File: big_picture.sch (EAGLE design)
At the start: 66 parts, among them IC1 LM555N

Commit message: updated big picture
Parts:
- removed ADD1, ADD2, BRAKE, HAZ_L, HAZ_R, HEAD, REAR, WIPER: PSMN039-100YS, nxp_60:PSMN039-100YS
- removed ADD1_SWITCH, ADD2_SWITCH, BRAKE_SENSOR, DAY_SWITCH, HAZ_L_SWITCH, HAZ_R_SWITCH, WIPER_SWITCH: (no value), switch:M9040P
- removed ADD2_OUT, ADD2_OUT1, ADD2_OUT2, ADD2_OUT3, ADD2_OUT4, ADD2_OUT5, ADD2_OUT6, ADD2_OUT7, VDD_IN: POWERPOLE_POWER25A, powerpoles:POWERPOLE_POWER25A
- removed C1: 33uF, rcl:C-USC0805
- removed C10, C8, C9: (no value), rcl:C-USC0805
- removed CONTACT: JJM2W-12V, relay:JJM2W-12V
- removed D1: (no value), diode:ZENER-DIODEDO34-7
- removed D2: 1N5817-B, diode:1N5817-B
- removed HORN: TL36WO, switch:TL36WO
- removed IC1: LM555N, linear:LM555N
- removed LED1, LED2, LED3, LED4, LED5, LED6, LED7, LED8: (no value), led:LEDCHIP-LED0805
- removed R1, R11, R2, R20, R21, R3, R4, R5, R6: 10K, rcl:R-US_R0805
- removed R10: 1K, rcl:R-US_R0805
- removed R12, R13, R14, R17, R18, R19, R9: (no value), rcl:R-US_R0805
- removed R15, R16: 220, rcl:R-US_R0805
- removed R7, R8: 0, rcl:R-US_R0805
- removed U$6: HORN, big_picture_parts:HORN
- added DZ1: LZR184, led:LZR184
- added E_STOP1: TL36WO, switch:TL36WO
- added G1: CR1/2, battery:CR1/2
- added K1: RELAY-SPDT-JZC-11F, SparkFun-Electromechanical:RELAY-SPDT-JZC-11F
- added M1: MOTOR10MM, SparkFun-Electromechanical:MOTOR10MM
- added S1: TL37PO, switch:TL37PO
- added SP1: AL30P, buzzer:AL30P
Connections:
- removed net 555_OUT: HAZ_L_SWITCH.P, HAZ_R_SWITCH.P, IC1.Q
- removed net GND: ADD1.S, ADD2.S, BRAKE.S, C1.2, C10.2, C8.2, C9.2, CONTACT2.NO2, D1.A, E_STOP.O, HAZ_L.S, HAZ_R.S, HEAD.S, HORN.O, IC1.GND, R1.2, R2.2, R20.1, R21.1, R3.2, R4.2, R5.2, R6.2, REAR.S, VDD_IN.GND, WIPER.S
- removed net H1: BRAKE_SENSOR.O, R17.1
- removed net H2: HAZ_R_SWITCH.O, R16.1
- removed net H3: HAZ_L_SWITCH.O, R15.1
- removed net H4: R14.1, WIPER_SWITCH.O
- removed net H5: ADD1_SWITCH.O, R13.1
- removed net H6: ADD2_SWITCH.O, R12.1
- removed net H7: DAY_SWITCH.O, R18.1, R19.1
- removed net N$10: LED7.C, R21.2
- removed net N$11: LED5.C, R5.1
- removed net N$12: HAZ_R.G, LED5.A, R16.2
- removed net N$13: BRAKE.G, LED6.A, R17.2
- removed net N$14: HEAD.G, LED7.A, R18.2
- removed net N$15: LED8.A, R19.2, REAR.G
- removed net N$16: ADD2_OUT.V+, R7.2
- removed net N$17: ADD1.D, ADD2_OUT1.GND
- removed net N$18: ADD2_OUT1.V+, R8.2
- removed net N$19: ADD2_OUT2.GND, D2.A, WIPER.D
- removed net N$20: ADD2_OUT2.V+, D2.C, R9.2
- removed net N$21: ADD2_OUT3.GND, HAZ_L.D
- removed net N$22: LED3.A, R14.2, WIPER.G
- removed net N$23: ADD2_OUT4.GND, HAZ_R.D
- removed net N$24: HAZ_L.G, LED4.A, R15.2
- removed net N$25: ADD2_OUT5.GND, BRAKE.D
- removed net N$26: ADD1.G, LED2.A, R13.2
- removed net N$27: LED1.C, R1.1
- removed net N$28: LED2.C, R2.1
- removed net N$29: LED4.C, R4.1
- removed net N$30: LED3.C, R3.1
- removed net N$33: LED6.C, R6.1
- removed net N$34: CONTACT1.1, CONTACT2.C, E_STOP.P, E_STOP.S, U$4.P$2
- removed net N$4: C1.1, IC1.THR, IC1.TR, R11.2
- removed net N$6: IC1.V+, R10.2
- removed net N$8: ADD2.D, ADD2_OUT.GND
- removed net N$9: LED8.C, R20.2
- removed net VDD: ADD1_SWITCH.P, ADD2_OUT3.V+, ADD2_OUT4.V+, ADD2_OUT5.V+, ADD2_OUT6.V+, ADD2_OUT7.V+, ADD2_SWITCH.P, BRAKE_SENSOR.P, CONTACT1.2, CONTACT2.NO1, DAY_SWITCH.P, VDD_IN.V+, WIPER_SWITCH.P
- removed net VDD_ADD1: C9.1, R8.1
- removed net VDD_ADD2: C8.1, R7.1
- removed net VDD_W: C10.1, D1.C, R9.1
- new net N$35: K1.NC, S1.S, U$4.P$1
- net N$1: now also E_STOP1.P, U$4.P$2, U$5.P$2; no longer ADD2_OUT6.GND, HEAD.D
- net N$2: now also G1.-; no longer HORN.P, U$6.P$1
- net N$3: now also E_STOP.P, E_STOP1.O; no longer ADD2_OUT7.GND, REAR.D
- net N$31: now also DZ1-1.A, DZ1-2.A, DZ1-3.A, DZ1-4.A, M1.+, SP1.2; no longer HORN.S
- net N$32: now also G1.+, K1.NO, S1.P; no longer U$4.P$1, U$5.P$2
- net N$5: now also DZ1-1.C, DZ1-2.C, DZ1-3.C, DZ1-4.C, M1.-, SP1.1; no longer IC1.DIS, R10.1, R11.1
- net N$7: now also E_STOP.O, K1.MAIN; no longer ADD2.G, LED1.A, R12.2
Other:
- note added: "48V- 12V Switching Regulator"
- note added: "AUX PDB"
- note added: "E-Stop Driver"
- note added: "E-Stop Exterior"
- note added: "Horn"
- note added: "MOM Push Button"
- note removed: "consider adding a trim pot in series with the resistor to fine tune the blinking rate"

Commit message: big picture
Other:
- note added: "48V"
- note added: "48V Contactor"
- note added: "Light Array"
- note added: "Wiper Motor"
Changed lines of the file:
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@@
 <text x="-83.82" y="66.04" size="1.778" layer="91">AUX PDB</text>
 <text x="-50.8" y="114.3" size="1.778" layer="91">48V- 12V Switching Regulator</text>
-<text x="-154.94" y="40.64" size="1.778" layer="91">Horn</text>
 <text x="-76.2" y="86.36" size="1.778" layer="91">E-Stop Driver</text>
 <text x="-53.34" y="86.36" size="1.778" layer="91">E-Stop Exterior</text>
 <text x="-106.68" y="152.4" size="1.778" layer="91">MOM Push Button</text>
+<text x="-134.62" y="38.1" size="1.778" layer="91">Wiper Motor</text>
+<text x="-104.14" y="17.78" size="1.778" layer="91">Light Array</text>
+<text x="-157.48" y="40.64" size="1.778" layer="91">Horn</text>
+<text x="-154.94" y="99.06" size="1.778" layer="91">48V</text>
+<text x="-106.68" y="124.46" size="1.778" layer="91">48V Contactor</text>
 </plain>
 <instances>
@@
 <instance part="U$5" gate="G$1" x="-78.74" y="58.42"/>
 <instance part="E_STOP" gate="BEF1" x="-68.58" y="78.74" smashed="yes" rot="R90"/>
-<instance part="G1" gate="1" x="-147.32" y="99.06" rot="R90"/>
+<instance part="G1" gate="1" x="-147.32" y="99.06" smashed="yes" rot="R90"/>
 <instance part="K1" gate="K$1" x="-99.06" y="111.76" smashed="yes" rot="R270">
 <attribute name="NAME" x="-91.186" y="119.38" size="1.778" layer="95" font="vector" rot="R270"/>
-<attribute name="VALUE" x="-111.252" y="124.46" size="1.778" layer="96" font="vector"/>
 </instance>
-<instance part="SP1" gate="G$1" x="-149.86" y="33.02" rot="R90"/>
+<instance part="SP1" gate="G$1" x="-149.86" y="33.02" smashed="yes" rot="R90">
+<attribute name="NAME" x="-156.21" y="29.21" size="1.778" layer="95" rot="R90"/>
+</instance>
 <instance part="S1" gate="BEF1" x="-99.06" y="144.78" rot="R270"/>
 <instance part="E_STOP1" gate="BEF1" x="-45.72" y="81.28" smashed="yes" rot="R90"/>
-<instance part="DZ1" gate="-1" x="-114.3" y="33.02"/>
-<instance part="DZ1" gate="-2" x="-104.14" y="33.02"/>
-<instance part="DZ1" gate="-3" x="-93.98" y="33.02"/>
-<instance part="DZ1" gate="-4" x="-83.82" y="33.02"/>
-<instance part="M1" gate="G$1" x="-137.16" y="33.02"/>
+<instance part="DZ1" gate="-1" x="-114.3" y="33.02" smashed="yes"/>
+<instance part="DZ1" gate="-2" x="-104.14" y="33.02" smashed="yes"/>
+<instance part="DZ1" gate="-3" x="-93.98" y="33.02" smashed="yes"/>
+<instance part="DZ1" gate="-4" x="-83.82" y="33.02" smashed="yes"/>
+<instance part="M1" gate="G$1" x="-137.16" y="33.02" smashed="yes"/>
 </instances>
 <busses>

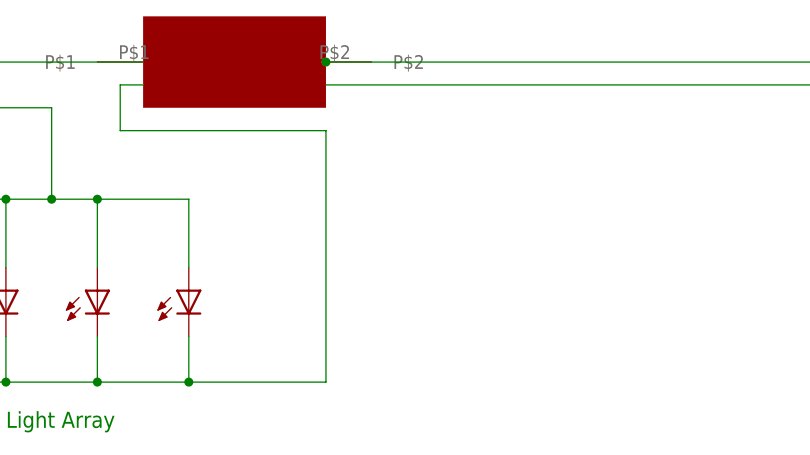
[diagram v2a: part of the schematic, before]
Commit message: added trim pot
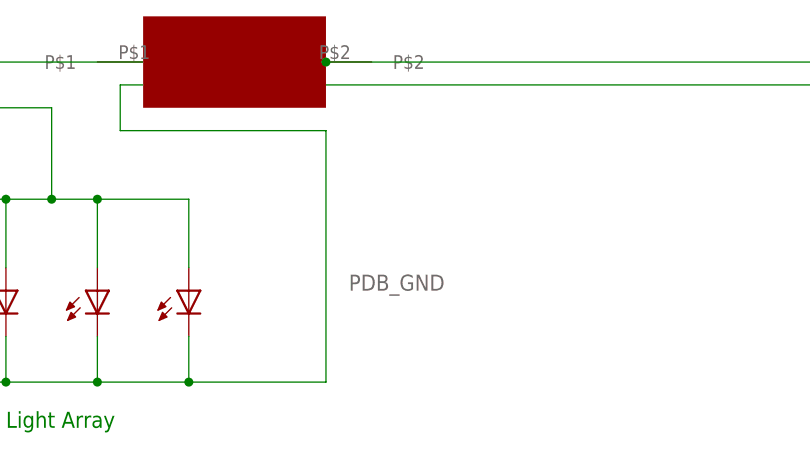
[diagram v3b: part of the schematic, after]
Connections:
- net N$5 renamed PDB_GND
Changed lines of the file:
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@@
 </segment>
 </net>
-<net name="N$5" class="0">
+<net name="PDB_GND" class="0">
 <segment>
 <wire x1="-88.9" y1="55.88" x2="-91.44" y2="55.88" width="0.1524" layer="91"/>
@@
 <wire x1="-83.82" y1="27.94" x2="-83.82" y2="22.86" width="0.1524" layer="91"/>
 <junction x="-83.82" y="22.86"/>
+<label x="-66.04" y="33.02" size="1.778" layer="95"/>
 </segment>
 </net>

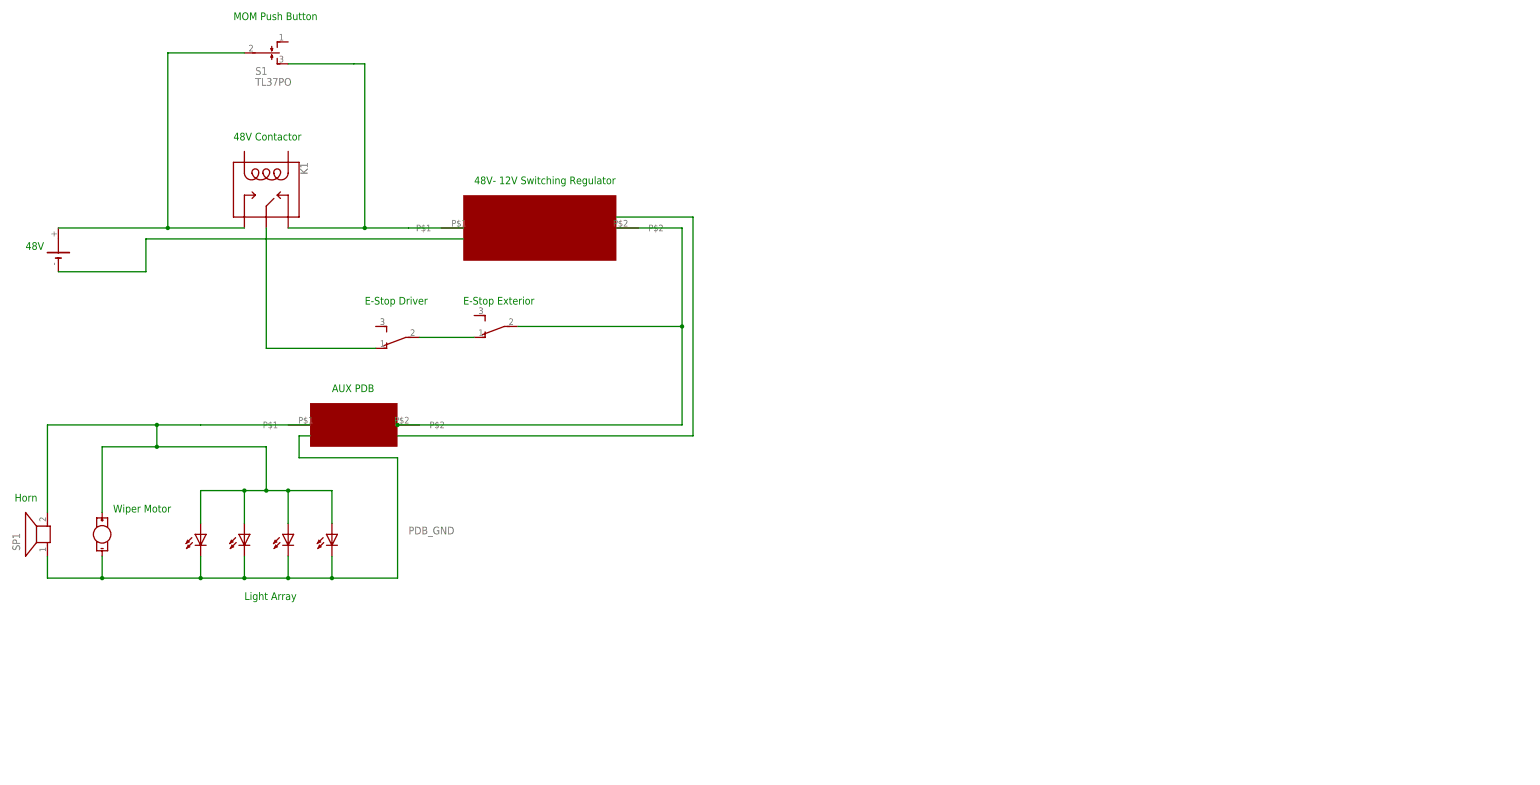
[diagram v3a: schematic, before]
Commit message: added custom part for buck
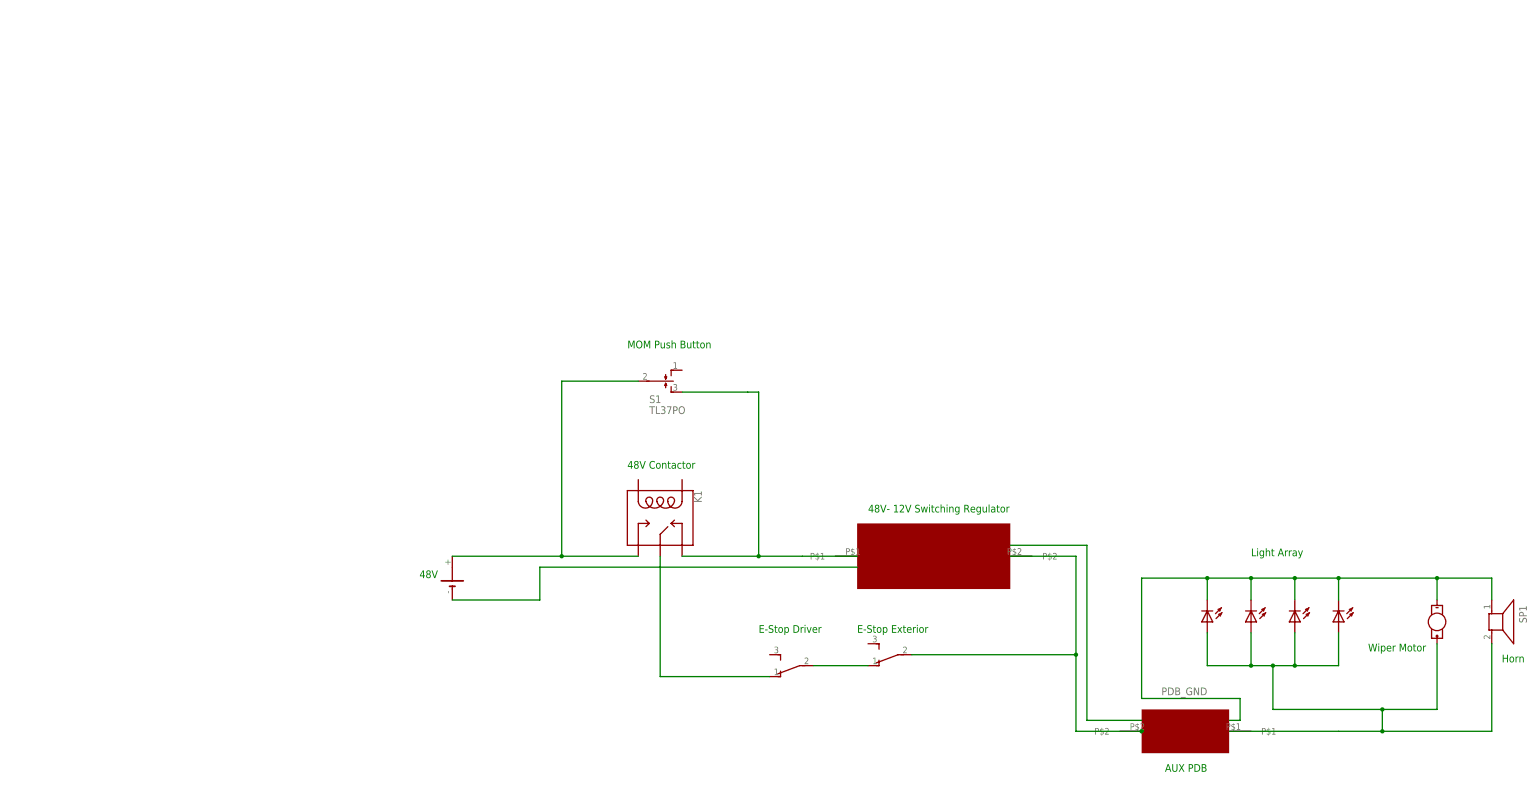
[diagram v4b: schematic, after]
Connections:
- new net N$5: U$5.P$2
- net N$1: no longer U$5.P$2
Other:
- moved on the sheet: K1, S1, SP1

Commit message: redid general schematic
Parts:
- U$4: value BUCK -> UEE150W; device big_picture_parts:BUCK -> REV Aux Circuit:UEE150W
- U$5: value AUX -> PDB_OUTLINE; device big_picture_parts:AUX -> REV Aux Circuit:PDB_OUTLINE
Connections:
- new net BRAKE_SENSOR: U$5.BRAKE_SENSOR
- new net N$10: U$4.V_OUT-, U$5.GND_IN
- new net N$4: G1.-, U$4.ON/OFF, U$4.V-
- new net N$8: DZ1-3.A, U$5.HEADLIGHT
- new net N$9: DZ1-2.A, U$5.TURN_SGN
- net N$1: now also U$4.V_OUT+, U$5.VCC; no longer U$4.P$2
- net N$2: now also DZ1-1.A, U$5.BRAKE_LIGHT; no longer G1.-
- net N$31: now also U$5.HORN; no longer DZ1-1.A, DZ1-2.A, DZ1-3.A, DZ1-4.A, M1.+, U$5.P$1
- net N$35: now also U$4.V+; no longer U$4.P$1
- net N$5: now also M1.+, U$5.WIPER; no longer U$5.P$2
- net PDB_GND: now also U$5.GND_OUT; no longer DZ1-4.C
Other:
- moved on the sheet: K1, S1, SP1

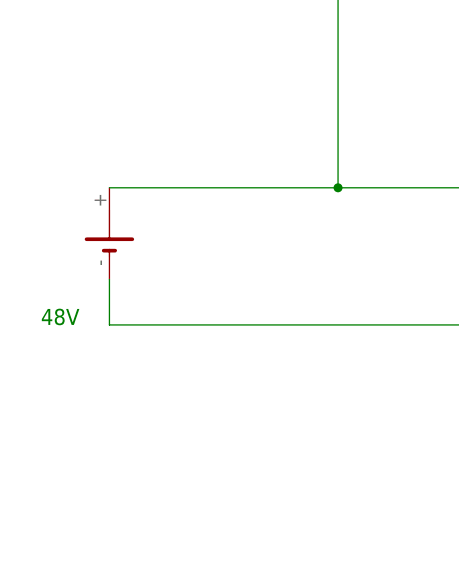
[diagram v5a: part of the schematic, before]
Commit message: improved layout of 555 timer
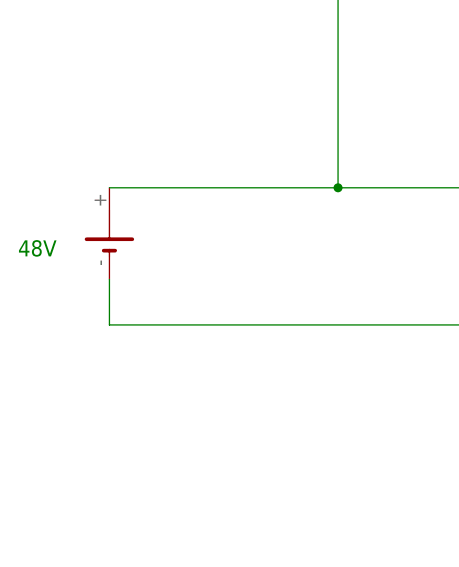
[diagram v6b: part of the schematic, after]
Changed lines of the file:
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@@
 <text x="-15.24" y="83.82" size="1.778" layer="91">MOM Push Button</text>
 <text x="25.4" y="-76.2" size="1.778" layer="91" rot="R180">Light Array</text>
-<text x="-63.5" y="22.86" size="1.778" layer="91">48V</text>
+<text x="-66.04" y="30.48" size="1.778" layer="91">48V</text>
 <text x="-15.24" y="58.42" size="1.778" layer="91">48V Contactor</text>
 <text x="76.2" y="-12.7" size="1.778" layer="91" rot="R180">AUX PDB</text>

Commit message: did initial route of PDB
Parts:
- added F3, FUSE_3A, FUSE_40A: FUSESH22,5A, fuse:FUSESH22,5A
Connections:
- removed net N$1: E_STOP1.P, U$4.V_OUT+, U$5.VCC
- new net FUSE_10A: E_STOP1.P, F3.1, F3.2, U$4.V_OUT+, U$5.VCC
- net N$32: now also FUSE_3A.1, FUSE_3A.2, FUSE_40A.1, FUSE_40A.2
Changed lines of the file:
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@@
 <part name="U$4" library="REV Aux Circuit" deviceset="UEE150W" device=""/>
 <part name="U$5" library="REV Aux Circuit" deviceset="PDB_OUTLINE" device=""/>
+<part name="FUSE_3A" library="fuse" library_urn="urn:adsk.eagle:library:233" deviceset="FUSE" device="SH22,5A" package3d_urn="urn:adsk.eagle:package:14070/1"/>
+<part name="FUSE_40A" library="fuse" library_urn="urn:adsk.eagle:library:233" deviceset="FUSE" device="SH22,5A" package3d_urn="urn:adsk.eagle:package:14070/1"/>
+<part name="F3" library="fuse" library_urn="urn:adsk.eagle:library:233" deviceset="FUSE" device="SH22,5A" package3d_urn="urn:adsk.eagle:package:14070/1"/>
 </parts>
 <sheets>
@@
 <text x="38.1" y="10.16" size="1.778" layer="91">E-Stop Exterior</text>
 <text x="-15.24" y="83.82" size="1.778" layer="91">MOM Push Button</text>
-<text x="25.4" y="-76.2" size="1.778" layer="91" rot="R180">Light Array</text>
+<text x="22.86" y="-76.2" size="1.778" layer="91" rot="R180">Light Array</text>
 <text x="-66.04" y="30.48" size="1.778" layer="91">48V</text>
 <text x="-15.24" y="58.42" size="1.778" layer="91">48V Contactor</text>
 <text x="76.2" y="-12.7" size="1.778" layer="91" rot="R180">AUX PDB</text>
-<text x="-15.24" y="-55.88" size="1.778" layer="91">Wiper Motor</text>
-<text x="-38.1" y="-53.34" size="1.778" layer="91">Horn</text>
+<text x="-22.86" y="-76.2" size="1.778" layer="91">Wiper Motor</text>
+<text x="-40.64" y="-66.04" size="1.778" layer="91">Horn</text>
 </plain>
 <instances>
@@
 <instance part="U$4" gate="G$1" x="50.8" y="17.78"/>
 <instance part="U$5" gate="G$1" x="60.96" y="-22.86" rot="R180"/>
+<instance part="FUSE_3A" gate="G$1" x="-30.48" y="63.5" smashed="yes" rot="R90">
+<attribute name="NAME" x="-31.877" y="59.69" size="1.778" layer="95" rot="R90"/>
+</instance>
+<instance part="FUSE_40A" gate="G$1" x="-45.72" y="38.1" smashed="yes" rot="R180">
+<attribute name="NAME" x="-41.91" y="36.703" size="1.778" layer="95" rot="R180"/>
+</instance>
+<instance part="F3" gate="G$1" x="99.06" y="-10.16" smashed="yes" rot="R270">
+<attribute name="NAME" x="100.457" y="-6.35" size="1.778" layer="95" rot="R270"/>
+</instance>
 </instances>
 <busses>
@@
 <pinref part="G1" gate="1" pin="+"/>
 <pinref part="K1" gate="K$1" pin="NO"/>
-<wire x1="-55.88" y1="38.1" x2="-30.48" y2="38.1" width="0.1524" layer="91"/>
+<wire x1="-55.88" y1="38.1" x2="-50.8" y2="38.1" width="0.1524" layer="91"/>
 <junction x="-30.48" y="38.1"/>
+<wire x1="-50.8" y1="38.1" x2="-40.64" y2="38.1" width="0.1524" layer="91"/>
+<wire x1="-40.64" y1="38.1" x2="-30.48" y2="38.1" width="0.1524" layer="91"/>
 <wire x1="-30.48" y1="38.1" x2="-12.7" y2="38.1" width="0.1524" layer="91"/>
-<wire x1="-30.48" y1="38.1" x2="-30.48" y2="78.74" width="0.1524" layer="91"/>
+<wire x1="-30.48" y1="38.1" x2="-30.48" y2="58.42" width="0.1524" layer="91"/>
 <pinref part="S1" gate="BEF1" pin="P"/>
+<wire x1="-30.48" y1="58.42" x2="-30.48" y2="68.58" width="0.1524" layer="91"/>
+<wire x1="-30.48" y1="68.58" x2="-30.48" y2="78.74" width="0.1524" layer="91"/>
 <wire x1="-30.48" y1="78.74" x2="-12.7" y2="78.74" width="0.1524" layer="91"/>
+<pinref part="FUSE_3A" gate="G$1" pin="2"/>
+<junction x="-30.48" y="68.58"/>
+<pinref part="FUSE_3A" gate="G$1" pin="1"/>
+<junction x="-30.48" y="58.42"/>
+<pinref part="FUSE_40A" gate="G$1" pin="2"/>
+<junction x="-50.8" y="38.1"/>
+<pinref part="FUSE_40A" gate="G$1" pin="1"/>
+<junction x="-40.64" y="38.1"/>
 </segment>
 </net>
@@
 </segment>
 </net>
-<net name="N$1" class="0">
+<net name="FUSE_10A" class="0">
 <segment>
 <wire x1="91.44" y1="40.64" x2="99.06" y2="40.64" width="0.1524" layer="91"/>
@@
 <junction x="99.06" y="5.08"/>
 <pinref part="U$4" gate="G$1" pin="V_OUT+"/>
-<wire x1="99.06" y1="5.08" x2="99.06" y2="-27.94" width="0.1524" layer="91"/>
+<wire x1="99.06" y1="5.08" x2="99.06" y2="-5.08" width="0.1524" layer="91"/>
 <pinref part="U$5" gate="G$1" pin="VCC"/>
+<wire x1="99.06" y1="-5.08" x2="99.06" y2="-15.24" width="0.1524" layer="91"/>
+<wire x1="99.06" y1="-15.24" x2="99.06" y2="-27.94" width="0.1524" layer="91"/>
 <wire x1="99.06" y1="-27.94" x2="93.98" y2="-27.94" width="0.1524" layer="91"/>
+<pinref part="F3" gate="G$1" pin="2"/>
+<junction x="99.06" y="-15.24"/>
+<pinref part="F3" gate="G$1" pin="1"/>
+<junction x="99.06" y="-5.08"/>
+<label x="101.6" y="-12.7" size="1.778" layer="95"/>
 </segment>
 </net>

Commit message: Built ESD
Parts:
- added E_STOP2: TL36WO, switch:TL36WO
- added MOTOR: MOTOR, master_library:MOTOR
- added U$6, U$8, U$9: SB50_BLOCK, master_library:SB50_BLOCK
- added U$7: MOTORCONTROLBLOCK, master_library:MOTORCONTROLBLOCK
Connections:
- removed net N$35: K1.NC, S1.S, U$4.V+
- removed net PDB_GND: DZ1-1.C, DZ1-2.C, DZ1-3.C, M1.-, SP1.1, U$5.GND_OUT
- new net GND: DZ1-1.C, DZ1-2.C, DZ1-3.C, G1.-, M1.-, SP1.1, U$5.GND_OUT, U$6.P$4, U$9.P$4
- new net N$1: U$7.MOTOR_OUT-, U$8.P$4
- new net N$11: E_STOP.O, E_STOP2.P
- new net N$12: U$6.P$1, U$7.BATTERY
- new net N$13: MOTOR.P$1, U$8.P$1
- new net N$14: MOTOR.P$2, U$8.P$2
- new net N$15: U$4.ON/OFF, U$4.V-, U$9.P$2
- new net N$16: K1.NC, S1.S, U$6.P$3, U$9.P$3
- new net N$17: U$4.V+, U$9.P$1
- new net N$6: U$7.MOTOR_OUT+, U$8.P$3
- new net PEDAL: U$7.PEDAL
- net N$4: now also U$6.P$2, U$7.GND; no longer G1.-, U$4.ON/OFF, U$4.V-
- net N$7: now also E_STOP2.O; no longer E_STOP.O
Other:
- note added: "Auxillary connected through MOLEX connector"
- note added: "Remote Cutoff"
- note added: "Rice Electric Vehicle Energy Supply Block Diagram"
